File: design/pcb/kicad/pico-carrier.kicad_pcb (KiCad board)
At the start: 2 copper layers, 90 x 113 mm, 29 parts, among them J1 TB6612FNG modulu, sol sira, J10 S7V7F5 5 V regulator, J2 TB6612FNG modulu, sag sira, J3 TOF400C sol, J4 TOF400C orta, J5 TOF400C sag, J6 MPU6050 (GY-521), J7 Sol motor + enkoder, J8 Sag motor + enkoder, J9 Pil girisi 4xAA, SW1 Guc anahtari (harici), U1 Raspberry Pi Pico 2 W

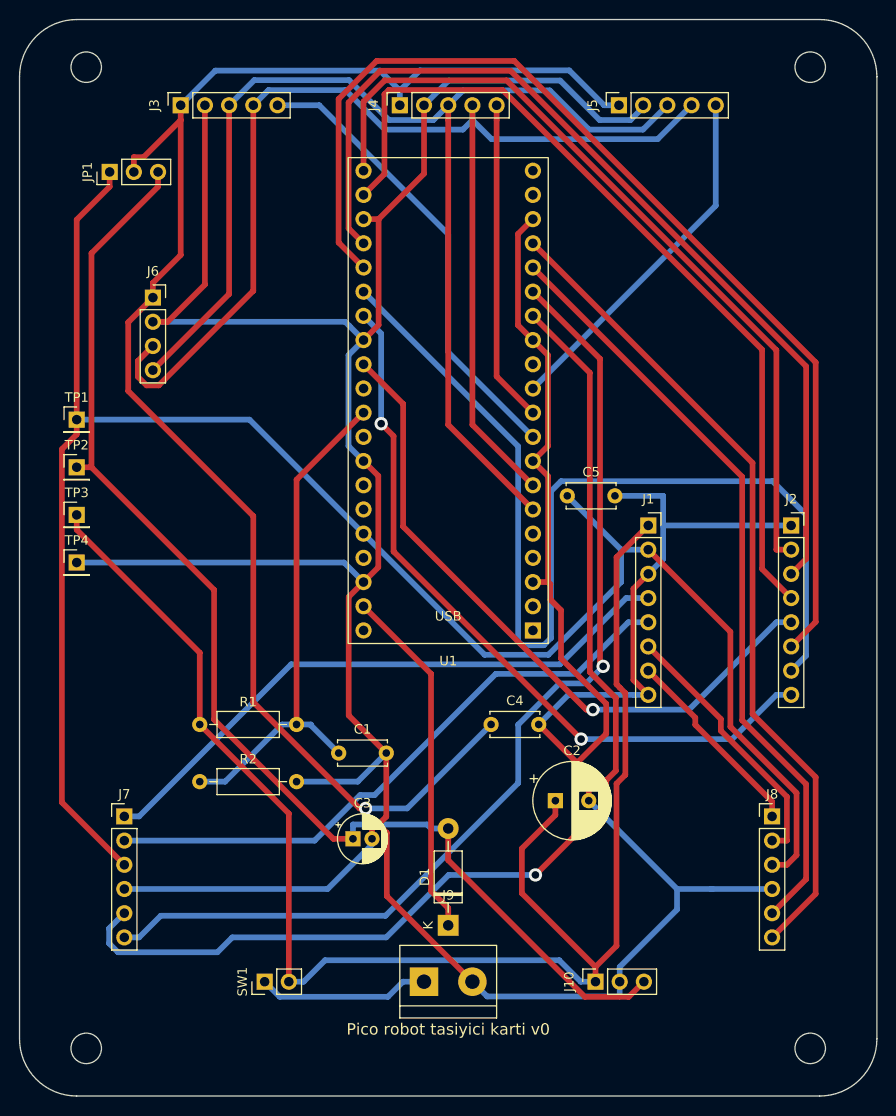
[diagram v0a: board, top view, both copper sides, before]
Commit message: Tek katmanli Pico karti (55 x 58): konnektor siralari, tek tel kopru, Freerouting job_timeout, tek katman testleri
Co-Authored-By: Claude Sonnet 5.5 <noreply@anthropic.com>
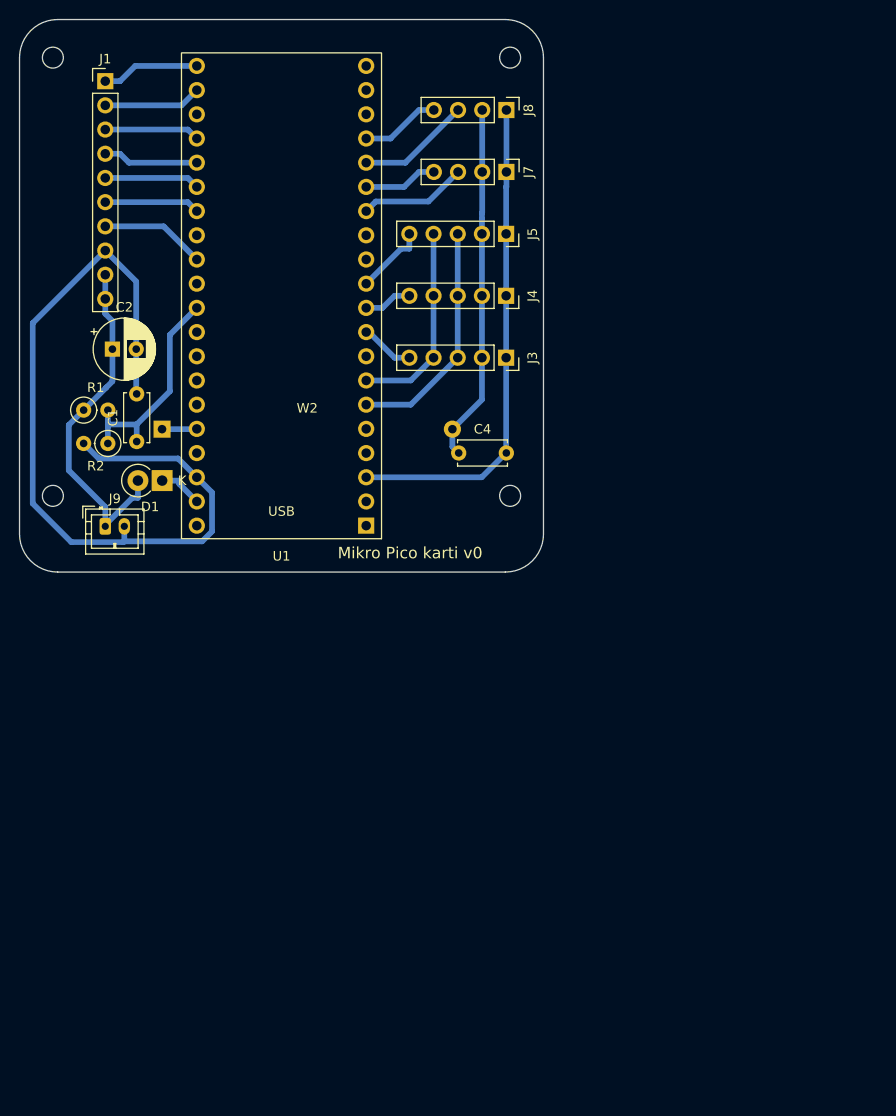
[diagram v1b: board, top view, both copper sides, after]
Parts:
- removed C3: 10 uF, Capacitor_THT:CP_Radial_D5.0mm_P2.00mm
- removed C5: 100 nF, Capacitor_THT:C_Disc_D5.0mm_W2.5mm_P5.00mm
- removed J10: S7V7F5 5 V regulator, Connector_PinSocket_2.54mm:PinSocket_1x03_P2.54mm_Vertical
- removed J2: TB6612FNG modulu, sag sira, Connector_PinSocket_2.54mm:PinSocket_1x08_P2.54mm_Vertical
- removed J6: MPU6050 (GY-521), Connector_PinSocket_2.54mm:PinSocket_1x04_P2.54mm_Vertical
- removed JP1: Sensor besleme secimi, Connector_PinHeader_2.54mm:PinHeader_1x03_P2.54mm_Vertical
- removed SW1: Guc anahtari (harici), Connector_PinHeader_2.54mm:PinHeader_1x02_P2.54mm_Vertical
- removed TP1: TP_3V3, Connector_PinHeader_2.54mm:PinHeader_1x01_P2.54mm_Vertical
- removed TP2: TP_5V, Connector_PinHeader_2.54mm:PinHeader_1x01_P2.54mm_Vertical
- removed TP3: TP_VM, Connector_PinHeader_2.54mm:PinHeader_1x01_P2.54mm_Vertical
- removed TP4: TP_GND, Connector_PinHeader_2.54mm:PinHeader_1x01_P2.54mm_Vertical
- added W2: Tel kopru 3V3, pico-carrier:WireLink_P30.48mm, F.Cu at (30.2, 43.0)
- C2: value 470 uF / 16 V -> 100 uF / 10 V; footprint Capacitor_THT:CP_Radial_D8.0mm_P3.50mm -> Capacitor_THT:CP_Radial_D6.3mm_P2.50mm
- D1: footprint Diode_THT:D_DO-41_SOD81_P10.16mm_Horizontal -> Diode_THT:D_DO-41_SOD81_P2.54mm_Vertical_KathodeUp
- H1, H2, H3, H4: value MountingHole_3.2mm_M3 -> MountingHole_2.2mm_M2; footprint MountingHole:MountingHole_3.2mm_M3 -> MountingHole:MountingHole_2.2mm_M2
- J1: value TB6612FNG modulu, sol sira -> Surucu baglantisi (TB6612); footprint Connector_PinSocket_2.54mm:PinSocket_1x08_P2.54mm_Vertical -> Connector_PinHeader_2.54mm:PinHeader_1x10_P2.54mm_Vertical
- J7: value Sol motor + enkoder -> Sol enkoder; footprint Connector_PinHeader_2.54mm:PinHeader_1x06_P2.54mm_Vertical -> Connector_PinHeader_2.54mm:PinHeader_1x04_P2.54mm_Vertical
- J8: value Sag motor + enkoder -> Sag enkoder; footprint Connector_PinHeader_2.54mm:PinHeader_1x06_P2.54mm_Vertical -> Connector_PinHeader_2.54mm:PinHeader_1x04_P2.54mm_Vertical
- J9: value Pil girisi 4xAA -> LiPo girisi (1S); footprint TerminalBlock:TerminalBlock_bornier-2_P5.08mm -> Connector_JST:JST_PH_B2B-PH-K_1x02_P2.00mm_Vertical
- R1: value 20 k -> 100 k; footprint Resistor_THT:R_Axial_DIN0207_L6.3mm_D2.5mm_P10.16mm_Horizontal -> Resistor_THT:R_Axial_DIN0207_L6.3mm_D2.5mm_P2.54mm_Vertical
- R2: value 10 k -> 100 k; footprint Resistor_THT:R_Axial_DIN0207_L6.3mm_D2.5mm_P10.16mm_Horizontal -> Resistor_THT:R_Axial_DIN0207_L6.3mm_D2.5mm_P2.54mm_Vertical
- moved J8 79.2 mm to (51.1, 9.50), turned to -90 degrees
- moved J7 78.6 mm to (51.1, 16.0), turned to -90 degrees
- moved J1 73.6 mm to (9.00, 6.47)
- moved C2 66.4 mm to (9.75, 34.6)
- moved H4 66.0 mm to (51.5, 50.0)
- moved J9 58.3 mm to (9.00, 53.2)
- moved H3 58.1 mm to (3.50, 50.0)
- moved D1 55.5 mm to (15.0, 48.4), turned to 180 degrees
- moved J3 43.2 mm to (51.1, 35.5), turned to -90 degrees
- moved C1 39.0 mm to (12.3, 44.3), turned to 90 degrees
- moved R2 36.8 mm to (9.27, 44.5), turned to 180 degrees
- moved R1 35.2 mm to (6.73, 41.0)
- moved H2 31.5 mm to (51.5, 4.00)
- moved C4 28.7 mm to (46.1, 45.5)
- moved J4 22.9 mm to (51.1, 29.0), turned to -90 degrees
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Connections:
- C4 pad 1: +SENS -> +3V3_L
- C4 pad 2: GND -> GND_L
- D1 pad 2: +5V -> VBAT_SW
- J1 pad 1: VBAT_SW -> PWMA
- J1 pad 2: +3V3 -> AIN1
- J1 pad 3: GND -> AIN2
- J1 pad 4: MOT_L+ -> BIN1
- J1 pad 5: MOT_L- -> BIN2
- J1 pad 6: MOT_R- -> PWMB
- J1 pad 7: MOT_R+ -> STBY
- J3 pad 1: +SENS -> GND_L
- J3 pad 2: GND -> +3V3_L
- J4 pad 1: +SENS -> GND_L
- J4 pad 2: GND -> +3V3_L
- J5 pad 1: +SENS -> GND_L
- J5 pad 2: GND -> +3V3_L
- J7 pad 1: MOT_L+ -> GND_L
- J7 pad 2: MOT_L- -> +3V3_L
- J7 pad 3: +3V3 -> ENC_L_A
- J7 pad 4: GND -> ENC_L_B
- J8 pad 1: MOT_R+ -> GND_L
- J8 pad 2: MOT_R- -> +3V3_L
- J8 pad 3: +3V3 -> ENC_R_A
- J8 pad 4: GND -> ENC_R_B
- J9 pad 1: VBAT_RAW -> VBAT_SW
- U1 pad 13: GND -> (no net)
- U1 pad 18: GND -> (no net)
- U1 pad 23: GND -> (no net)
- U1 pad 28: GND -> (no net)
- U1 pad 3: GND -> GND_L
- U1 pad 33: GND -> (no net)
- U1 pad 8: GND -> (no net)
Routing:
- net GND: track 436.2 -> 88.4 mm
- net +3V3: track 203.8 -> 3.66 mm
- net +SENS: track 164.0 -> 0.00 mm, vias 1 -> 0
- net +5V: track 129.2 -> 0.00 mm
- net VBAT_SW: track 165.3 -> 36.7 mm
- net I2C_SCL: track 135.1 -> 21.1 mm
- net ENC_L_A: track 118.1 -> 11.3 mm, vias 1 -> 0
- net I2C_SDA: track 130.1 -> 24.7 mm
- net BIN1: track 114.5 -> 10.00 mm
- net ENC_L_B: track 108.0 -> 7.75 mm, vias 1 -> 0
- net BIN2: track 108.5 -> 10.00 mm
- net AIN2: track 100.1 -> 10.00 mm
- net AIN1: track 89.9 -> 10.3 mm
- net ENC_R_B: track 87.0 -> 8.34 mm
- net PWMA: track 85.7 -> 10.3 mm
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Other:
- board size 90 x 113 mm -> 55 x 58 mm
- board text added: "Mikro Pico karti v0"
- board text removed: "Pico robot tasiyici karti v0"
